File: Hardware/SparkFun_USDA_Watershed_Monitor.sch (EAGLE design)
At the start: 114 parts, among them J10 QWIIC_RIGHT_ANGLE, J3 QWIIC_RIGHT_ANGLE, J4 U.FL, J5 RJ45, J7 RJ45, J9 RJ45, Q1 20V/4.2A/52mΩ/1.4W, Q2 20V/0.2A/8MHz/1.2Ω/1Vth, Q3 20V/0.2A/8MHz/1.2Ω/1Vth, Q4 20V/0.2A/8MHz/1.2Ω/1Vth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

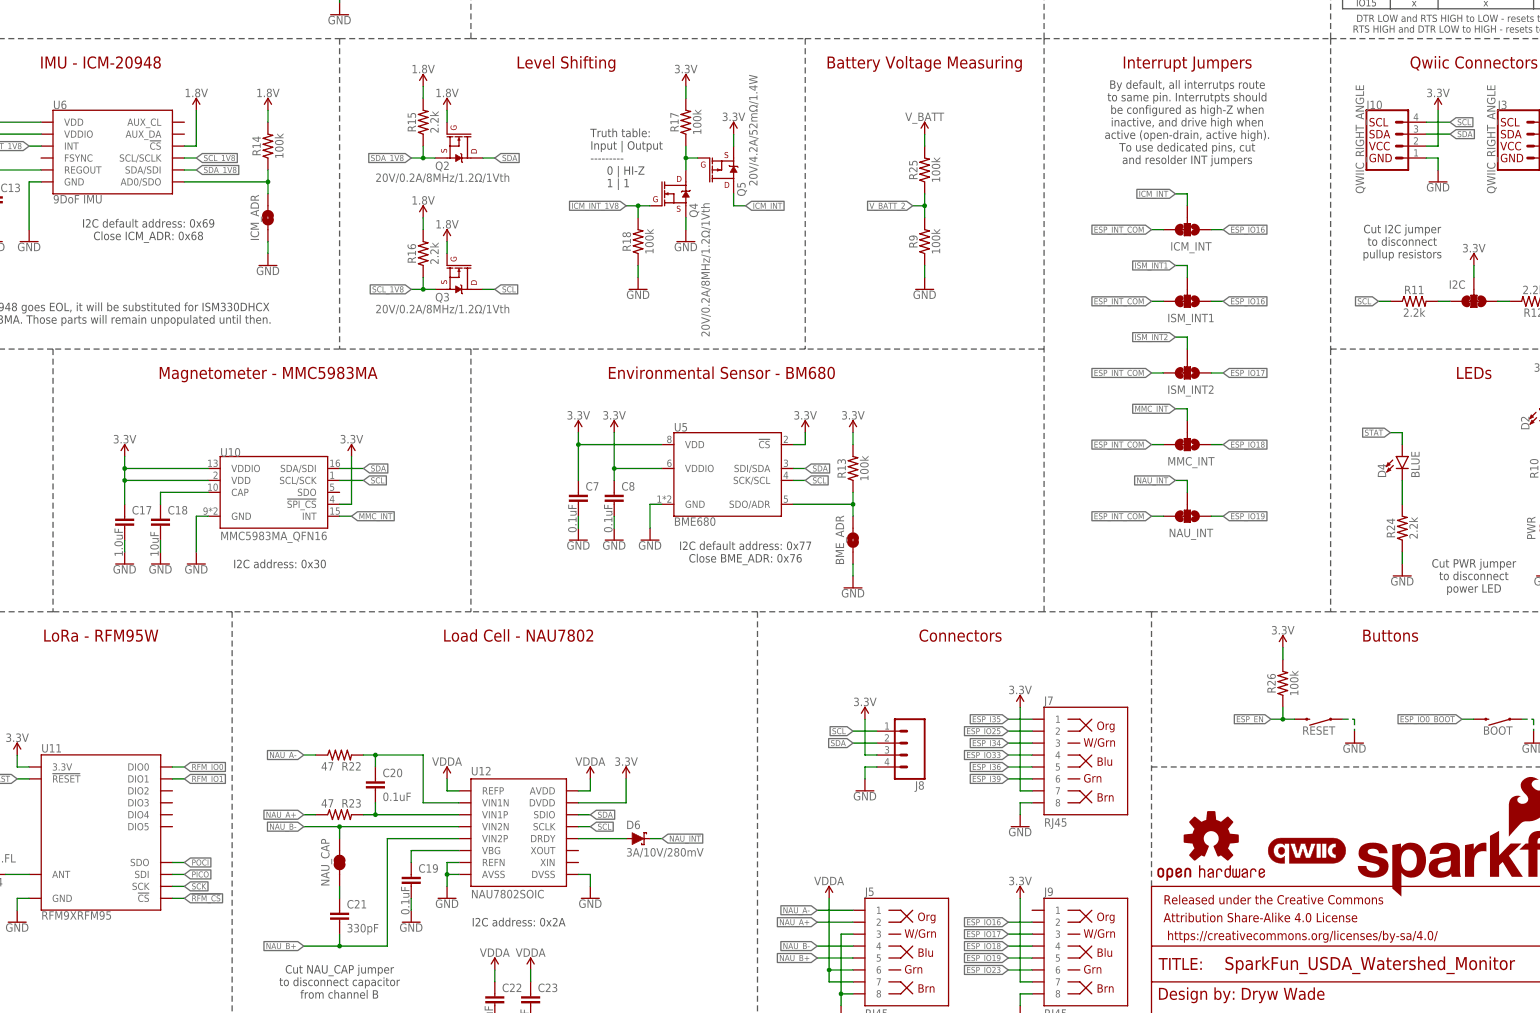
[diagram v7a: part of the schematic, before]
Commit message: Add VOUT net for GPIO A, left Qwiic, and load cell
Controlled by a P-channel MOSFET, had to steal GPIO16
Also changed "5V" label to "5V IN"
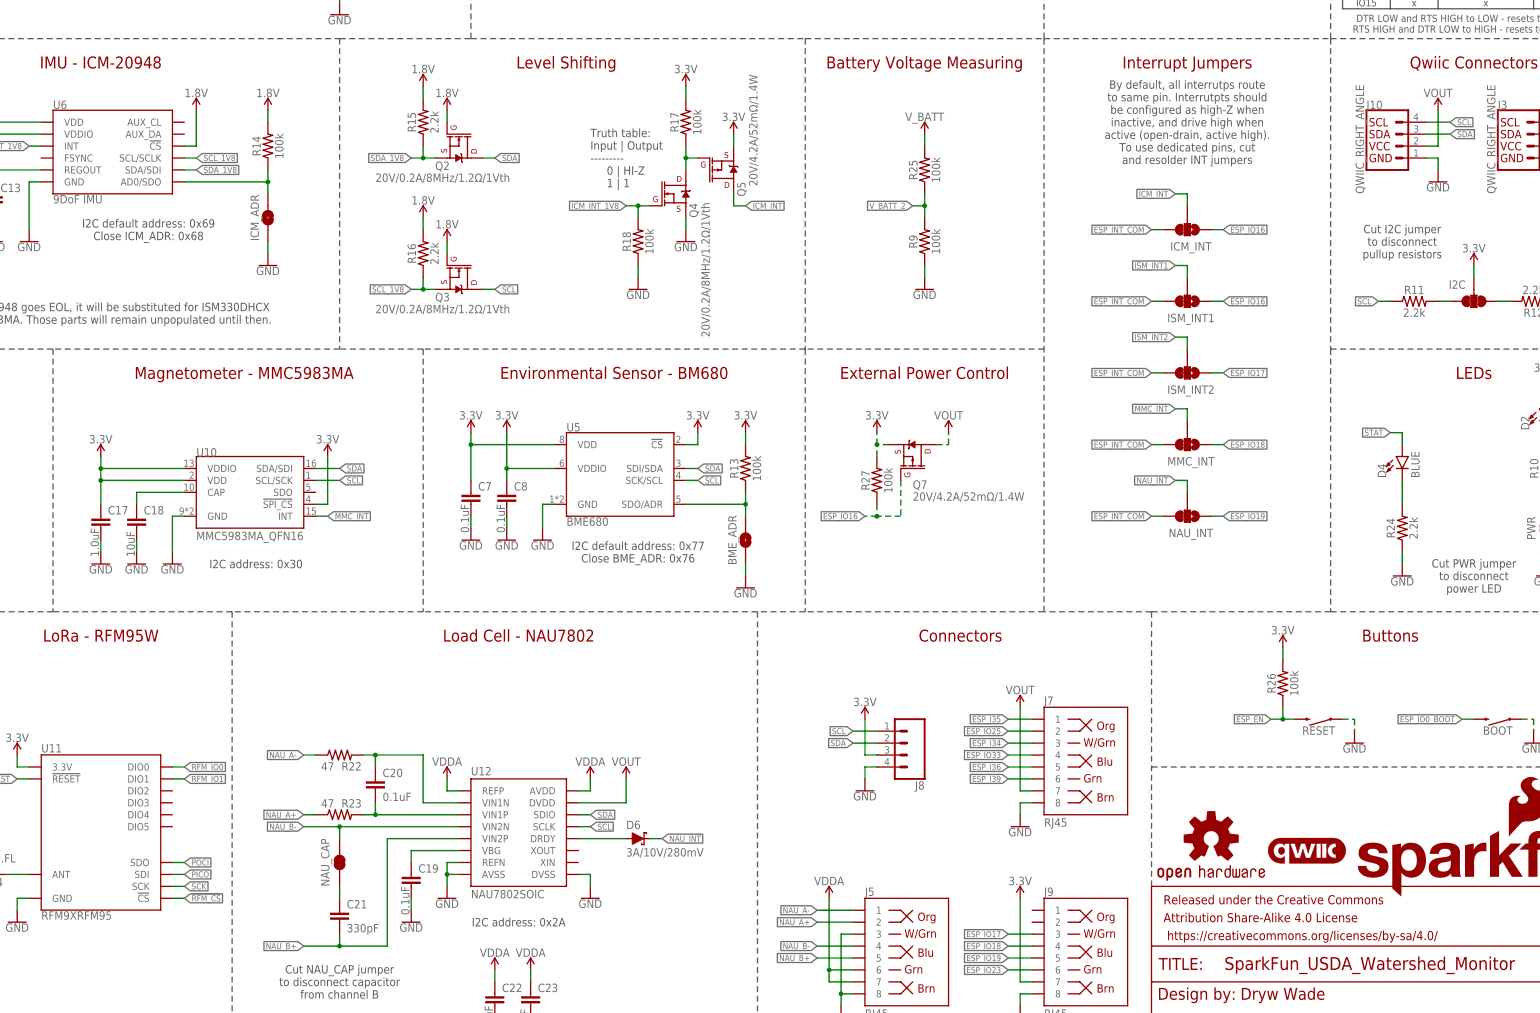
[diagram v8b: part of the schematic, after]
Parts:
- added Q7: 20V/4.2A/52mΩ/1.4W, SparkFun-DiscreteSemi:MOSFET_PCH-DMG2305UX-7
- added R27: 100k, SparkFun-Resistors:100KOHM-0603-1/10W-1%
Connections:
- new net VOUT: J10.2, J7.7, Q7.D, U12.DVDD
- net 3.3V: now also Q7.S, R27.2; no longer J10.2, J7.7, U12.DVDD
- net ESP_IO16: now also Q7.G, R27.1; no longer J9.2
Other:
- note added: "External Power Control"
- moved on the sheet: BME_ADR, C17, C18, C7, C8, R13, U10, U5
